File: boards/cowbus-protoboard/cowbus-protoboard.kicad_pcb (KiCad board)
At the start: 2 copper layers, 68.7 x 63.7 mm, 44 parts, among them P1 CPU_TO_PERIPH, P2 PERIPH_TO_MCU, P3 SWD, P4 BUZ, P5 USART_DEBUG, P6 CONN_01X02, SW1 SW1, SW2 SW2, SW3 SW3, SW4 SW4, U1 STM32F030C8T6, U2 TS5204, U3 nRF24L01+-Module, U4 24C16, U5 LM75AD, Y1 8MHz, Y2 32,768kHz

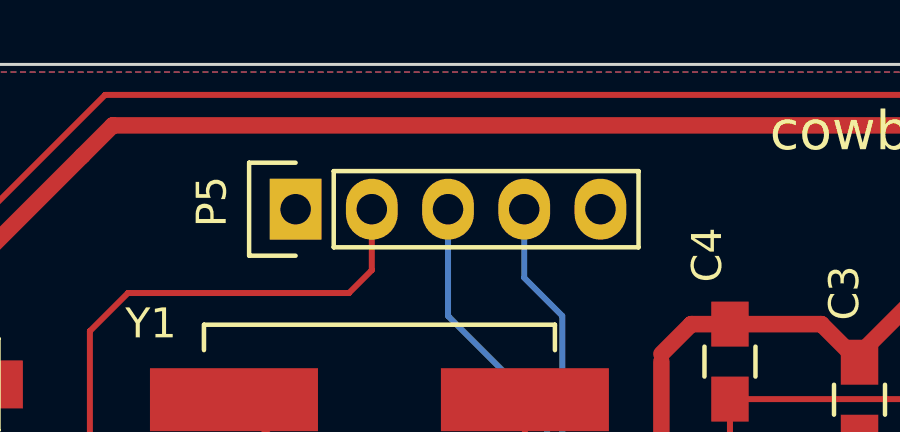
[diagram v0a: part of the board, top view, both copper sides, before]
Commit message: protoboard: added debug_uart pin markers
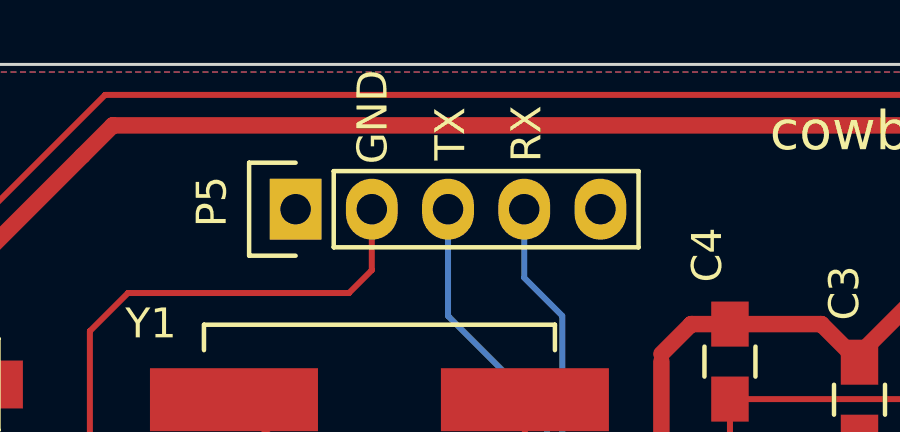
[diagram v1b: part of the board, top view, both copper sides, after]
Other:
- board text added: "GND"
- board text added: "RX"
- board text added: "TX"
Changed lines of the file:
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@@
-(kicad_pcb (version 4) (host pcbnew 0.201508090901+6074~28~ubuntu14.04.1-product)
+(kicad_pcb (version 4) (host pcbnew 0.201508130901+6089~28~ubuntu14.04.1-product)
   (general
     (links 143)
@@
     (area 114.707999 69.440899 194.715933 138.962601)
     (thickness 1.6)
-    (drawings 9)
+    (drawings 12)
     (tracks 812)
     (zones 0)
@@
   (title_block
     (title "cowbus protoboard")
-    (date 2015-08-02)
-    (rev 1)
+    (date 2015-08-15)
+    (rev 1.1)
   )
   (layers
@@
     (fp_line (start 0.35052 0.89916) (end 0.7493 1.89992) (layer F.SilkS) (width 0.15))
   )
+  (gr_text RX (at 142.8242 77.4954 90) (layer F.SilkS)
+    (effects (font (size 1 1) (thickness 0.18)))
+  )
+  (gr_text TX (at 140.2842 77.4954 90) (layer F.SilkS)
+    (effects (font (size 1 1) (thickness 0.18)))
+  )
+  (gr_text GND (at 137.6934 76.9366 90) (layer F.SilkS)
+    (effects (font (size 1 1) (thickness 0.18)))
+  )
   (dimension 63.601783 (width 0.3) (layer F.SilkS)

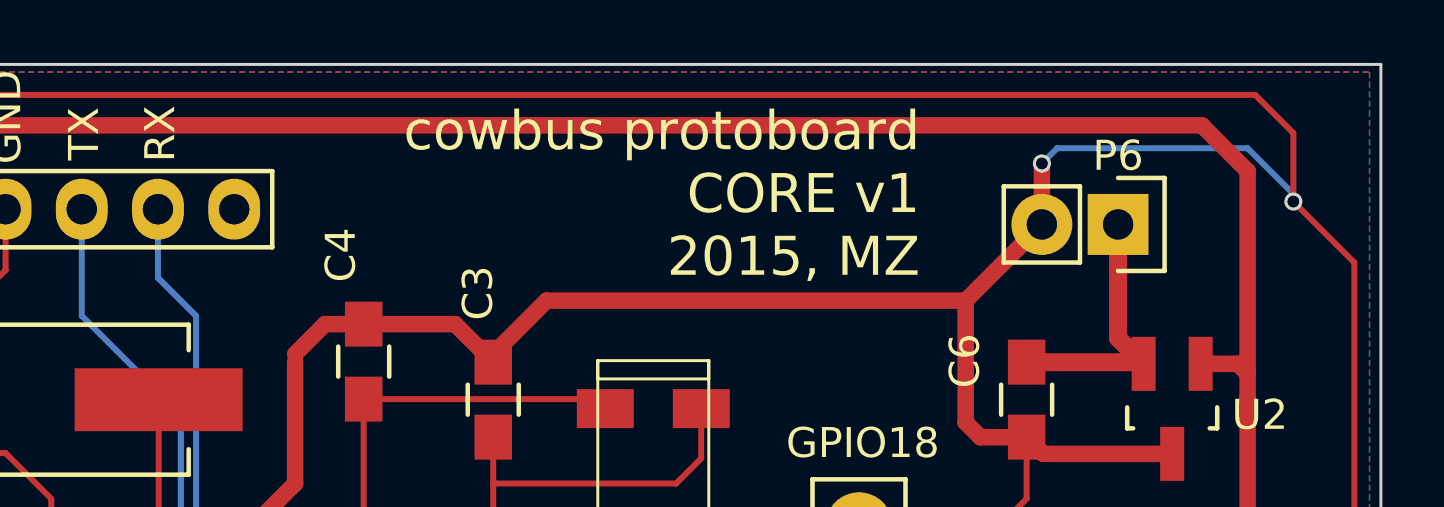
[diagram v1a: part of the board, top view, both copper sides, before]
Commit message: protoboard: added V_in markers (GND, voltage)
+ updated gerber and PDF files
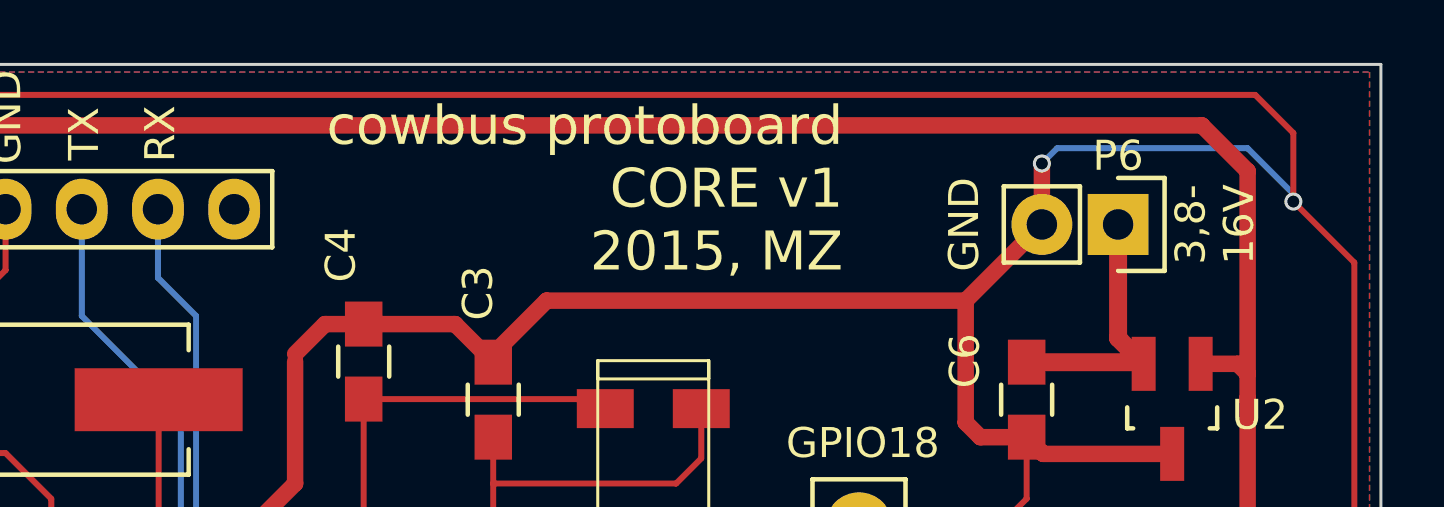
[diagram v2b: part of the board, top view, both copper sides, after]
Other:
- board text added: "3,8- 16V"
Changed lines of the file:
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@@
     (area 114.707999 69.440899 194.715933 138.962601)
     (thickness 1.6)
-    (drawings 12)
+    (drawings 14)
     (tracks 812)
     (zones 0)
@@
     (visible_elements FFFEEF7F)
     (pcbplotparams
-      (layerselection 0x030fc_80000001)
+      (layerselection 0x010fc_80000001)
       (usegerberextensions false)
       (excludeedgelayer true)
@@
       (padsonsilk false)
       (subtractmaskfromsilk false)
-      (outputformat 1)
+      (outputformat 4)
       (mirror false)
       (drillshape 0)
       (scaleselection 1)
-      (outputdirectory gerber/))
+      (outputdirectory pdf/layout/))
   )
   (net 0 "")
@@
     (fp_line (start 0.35052 0.89916) (end 0.7493 1.89992) (layer F.SilkS) (width 0.15))
   )
+  (gr_text "3,8-\n16V" (at 177.9778 80.518 90) (layer F.SilkS)
+    (effects (font (size 1 1) (thickness 0.18)))
+  )
+  (gr_text GND (at 169.6212 80.518 90) (layer F.SilkS)
+    (effects (font (size 1 1) (thickness 0.18)))
+  )
   (gr_text RX (at 142.8242 77.4954 90) (layer F.SilkS)
     (effects (font (size 1 1) (thickness 0.18)))
@@
     (arrow2b (pts (xy 114.803317 72.367096) (xy 115.928514 71.778172)))
   )
-  (gr_text "cowbus protoboard\nCORE v1\n2015, MZ" (at 168.148 79.502) (layer F.SilkS)
+  (gr_text "cowbus protoboard\nCORE v1\n2015, MZ" (at 165.5826 79.3242) (layer F.SilkS)
     (effects (font (size 1.3 1.3) (thickness 0.25)) (justify right))
   )
